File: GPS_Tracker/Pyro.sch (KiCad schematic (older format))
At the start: 1 part

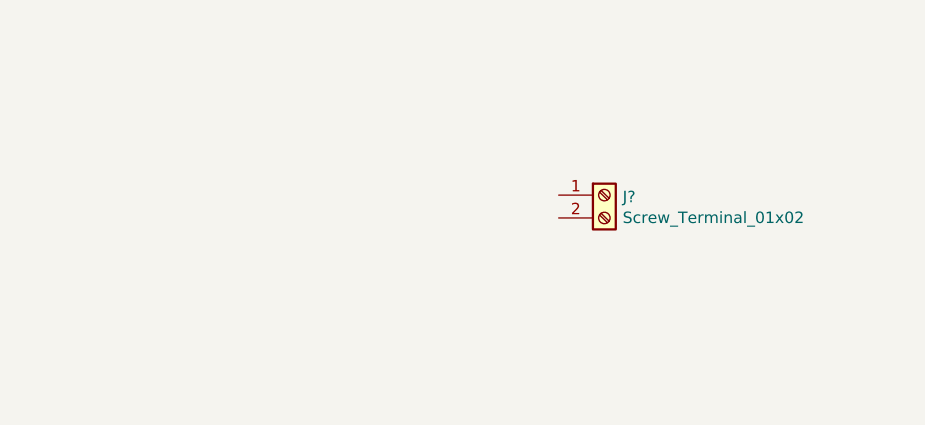
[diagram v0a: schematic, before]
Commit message: added example pyro
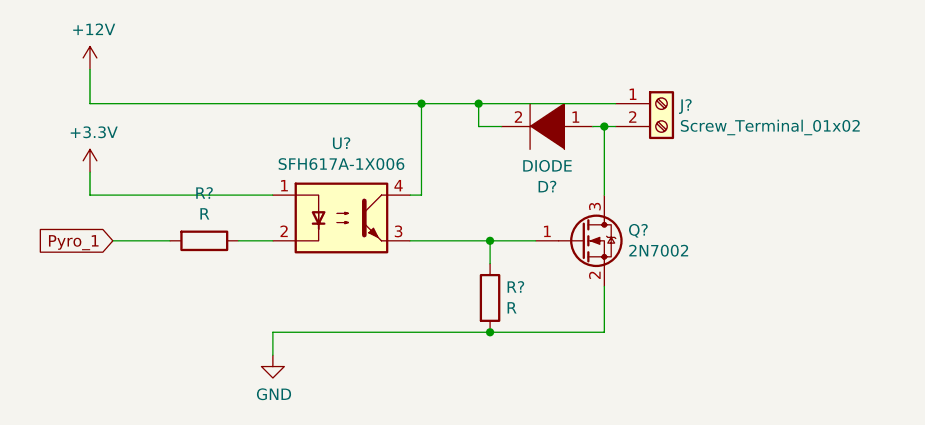
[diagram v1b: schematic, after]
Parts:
- added D?: DIODE, symbol pspice:DIODE
- added Q?: 2N7002, Package_TO_SOT_SMD:SOT-23, symbol Transistor_FET:2N7002
- added R? (x2): R, symbol Device:R
- added U?: SFH617A-1X006, Package_DIP:DIP-4_W10.16mm, symbol Isolator:SFH617A-1X006
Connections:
- net +12V: now reaches J?.1 (Pin_1)
- net +12V: now also D?.2 (A), U?.4
- net at J?.2 (Pin_2): now also D?.1 (K), Q?.3 (D)
- new net: R?.1, U?.2
- new net: Q?.1 (G), R?.1, U?.3
- new net +3V3: U?.1
- new net GND: Q?.2 (S), R?.2
- new net Pyro_1: R?.2
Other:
- moved on the sheet: J?
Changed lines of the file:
@@
 L Connector:Screw_Terminal_01x02 J?
 U 1 1 5E714A66
-P 5900 3250
-F 0 "J?" H 5980 3242 50  0000 L CNN
-F 1 "Screw_Terminal_01x02" H 5980 3151 50  0000 L CNN
-F 2 "" H 5900 3250 50  0001 C CNN
-F 3 "~" H 5900 3250 50  0001 C CNN
-	1    5900 3250
+P 6150 2850
+F 0 "J?" H 6230 2842 50  0000 L CNN
+F 1 "Screw_Terminal_01x02" H 6230 2751 50  0000 L CNN
+F 2 "" H 6150 2850 50  0001 C CNN
+F 3 "~" H 6150 2850 50  0001 C CNN
+	1    6150 2850
 	1    0    0    -1
 $EndComp
+Text GLabel 3750 3450 0    50   Input ~ 0
+Pyro_1
+$Comp
+L Isolator:SFH617A-1X006 U?
+U 1 1 5E7165FB
+P 4750 3350
+F 0 "U?" H 4750 3675 50  0000 C CNN
+F 1 "SFH617A-1X006" H 4750 3584 50  0000 C CNN
+F 2 "Package_DIP:DIP-4_W10.16mm" H 4550 3150 50  0001 L CIN
+F 3 "http://www.vishay.com/docs/83740/sfh617a.pdf" H 4750 3350 50  0001 L CNN
+	1    4750 3350
+	1    0    0    -1
+$EndComp
+$Comp
+L Device:R R?
+U 1 1 5E717F77
+P 4150 3450
+F 0 "R?" V 3943 3450 50  0000 C CNN
+F 1 "R" V 4034 3450 50  0000 C CNN
+F 2 "" V 4080 3450 50  0001 C CNN
+F 3 "~" H 4150 3450 50  0001 C CNN
+	1    4150 3450
+	0    1    1    0
+$EndComp
+$Comp
+L power:+3.3V #PWR?
+U 1 1 5E718B0F
+P 3650 3150
+F 0 "#PWR?" H 3650 3000 50  0001 C CNN
+F 1 "+3.3V" H 3665 3323 50  0000 C CNN
+F 2 "" H 3650 3150 50  0001 C CNN
+F 3 "" H 3650 3150 50  0001 C CNN
+	1    3650 3150
+	1    0    0    -1
+$EndComp
+Wire Wire Line
+	3750 3450 4000 3450
+Wire Wire Line
+	4300 3450 4450 3450
+Wire Wire Line
+	4450 3250 3650 3250
+Wire Wire Line
+	3650 3250 3650 3150
+$Comp
+L power:+12V #PWR?
+U 1 1 5E71C719
+P 3650 2700
+F 0 "#PWR?" H 3650 2550 50  0001 C CNN
+F 1 "+12V" H 3665 2873 50  0000 C CNN
+F 2 "" H 3650 2700 50  0001 C CNN
+F 3 "" H 3650 2700 50  0001 C CNN
+	1    3650 2700
+	1    0    0    -1
+$EndComp
+$Comp
+L pspice:DIODE D?
+U 1 1 5E71D693
+P 5650 2950
+F 0 "D?" H 5650 3215 50  0000 C CNN
+F 1 "DIODE" H 5650 3124 50  0000 C CNN
+F 2 "" H 5650 2950 50  0001 C CNN
+F 3 "~" H 5650 2950 50  0001 C CNN
+	1    5650 2950
+	-1   0    0    1
+$EndComp
+Wire Wire Line
+	5950 2850 5350 2850
+Wire Wire Line
+	3650 2850 3650 2700
+Wire Wire Line
+	5050 3250 5100 3250
+Wire Wire Line
+	5100 3250 5100 2850
+Connection ~ 5100 2850
+Wire Wire Line
+	5100 2850 3650 2850
+$Comp
+L power:GND #PWR?
+U 1 1 5E723142
+P 4450 3950
+F 0 "#PWR?" H 4450 3700 50  0001 C CNN
+F 1 "GND" H 4455 3777 50  0000 C CNN
+F 2 "" H 4450 3950 50  0001 C CNN
+F 3 "" H 4450 3950 50  0001 C CNN
+	1    4450 3950
+	1    0    0    -1
+$EndComp
+Wire Wire Line
+	5950 2950 5900 2950
+Wire Wire Line
+	5450 2950 5350 2950
+Wire Wire Line
+	5350 2950 5350 2850
+Connection ~ 5350 2850
+Wire Wire Line
+	5350 2850 5100 2850
+$Comp
+L Transistor_FET:2N7002 Q?
+U 1 1 5E72466D
+P 5800 3450
+F 0 "Q?" H 6004 3496 50  0000 L CNN
+F 1 "2N7002" H 6004 3405 50  0000 L CNN
+F 2 "Package_TO_SOT_SMD:SOT-23" H 6000 3375 50  0001 L CIN
+F 3 "https://www.fairchildsemi.com/datasheets/2N/2N7002.pdf" H 5800 3450 50  0001 L CNN
+	1    5800 3450
+	1    0    0    -1
+$EndComp
+Wire Wire Line
+	5050 3450 5400 3450
+Wire Wire Line
+	5900 3250 5900 2950
+Connection ~ 5900 2950
+Wire Wire Line
+	5900 2950 5850 2950
+$Comp
+L Device:R R?
+U 1 1 5E72D6EC
+P 5400 3700
+F 0 "R?" H 5470 3746 50  0000 L CNN
+F 1 "R" H 5470 3655 50  0000 L CNN
+F 2 "" V 5330 3700 50  0001 C CNN
+F 3 "~" H 5400 3700 50  0001 C CNN
+	1    5400 3700
+	1    0    0    -1
+$EndComp
+Wire Wire Line
+	5400 3550 5400 3450
+Connection ~ 5400 3450
+Wire Wire Line
+	5400 3450 5600 3450
+Wire Wire Line
+	4450 3950 4450 3850
+Wire Wire Line
+	4450 3850 5400 3850
+Wire Wire Line
+	5400 3850 5900 3850
+Wire Wire Line
+	5900 3850 5900 3650
+Connection ~ 5400 3850
 $EndSCHEMATC
